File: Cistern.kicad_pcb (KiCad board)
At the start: 2 copper layers, 55.5 x 79.6 mm, 15 parts, among them J2 Gauge Stepper, J3 Power Connector, Q1 BD244C, SW1 WiFi reset, SW2 Water Sensor, U1 ULN2003A, U3 Boost Converter (5->20 V)

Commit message: Changing pin assignments to make things work
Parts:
- SW1: value WiFi reset -> WiFi reset switch
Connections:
- MCU1 pad 13: unconnected-(MCU1-GPIO13-Pad13) -> Net-(MCU1-GPIO13)
- MCU1 pad 5: Net-(MCU1-GPIO35) -> unconnected-(MCU1-GPIO35-Pad5)
- U1 pad 1: Net-(MCU1-GPIO27) -> Net-(MCU1-GPIO13)
- U1 pad 2: Net-(MCU1-GPIO26) -> Net-(MCU1-GPIO27)
- U1 pad 3: Net-(MCU1-GPIO25) -> Net-(MCU1-GPIO26)
- U1 pad 4: Net-(MCU1-GPIO33) -> Net-(MCU1-GPIO25)
- U1 pad 5: Net-(MCU1-GPIO32) -> Net-(MCU1-GPIO33)
- U1 pad 6: Net-(MCU1-GPIO35) -> Net-(MCU1-GPIO32)
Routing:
- net Net-(MCU1-GPIO13): track 0.00 -> 17.8 mm
- net Net-(MCU1-GPIO35): track 10.2 -> 0.00 mm
- net Net-(D2-A): track 10.8 -> 8.94 mm
- net Net-(MCU1-GPIO27): track 10.2 -> 11.2 mm
- net Net-(MCU1-GPIO25): track 10.2 -> 11.2 mm
- net Net-(MCU1-GPIO33): track 10.2 -> 11.2 mm
- net Net-(MCU1-GPIO32): track 10.2 -> 11.2 mm
- net Net-(MCU1-GPIO26): track 10.2 -> 11.2 mm
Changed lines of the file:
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@@
 	(net 15 "unconnected-(MCU1-GPIO21-Pad20)")
 	(net 16 "unconnected-(MCU1-RX2-Pad25)")
-	(net 17 "Net-(MCU1-GPIO35)")
+	(net 17 "Net-(MCU1-GPIO13)")
 	(net 18 "unconnected-(MCU1-VN-Pad3)")
 	(net 19 "unconnected-(MCU1-3V3-Pad30)")
@@
 	(net 24 "unconnected-(MCU1-GPIO23-Pad16)")
 	(net 25 "unconnected-(MCU1-GPIO5-Pad23)")
-	(net 26 "unconnected-(MCU1-GPIO13-Pad13)")
+	(net 26 "unconnected-(MCU1-GPIO35-Pad5)")
 	(net 27 "unconnected-(MCU1-TX0-Pad18)")
 	(net 28 "unconnected-(MCU1-TX2-Pad24)")
@@
 			)
 		)
-		(property "Value" "WiFi reset"
+		(property "Value" "WiFi reset switch"
 			(at 2.54 -2.54 180)
 			(layer "F.Fab")
@@
 			(layers "*.Cu" "*.Mask")
 			(remove_unused_layers no)
-			(net 20 "Net-(MCU1-GPIO27)")
+			(net 17 "Net-(MCU1-GPIO13)")
 			(pinfunction "I1")
 			(pintype "input")
@@
 			(layers "*.Cu" "*.Mask")
 			(remove_unused_layers no)
-			(net 11 "Net-(MCU1-GPIO26)")
+			(net 20 "Net-(MCU1-GPIO27)")
 			(pinfunction "I2")
 			(pintype "input")
@@
 			(layers "*.Cu" "*.Mask")
 			(remove_unused_layers no)
-			(net 35 "Net-(MCU1-GPIO25)")
+			(net 11 "Net-(MCU1-GPIO26)")
 			(pinfunction "I3")
 			(pintype "input")
@@
 			(layers "*.Cu" "*.Mask")
 			(remove_unused_layers no)
-			(net 12 "Net-(MCU1-GPIO33)")
+			(net 35 "Net-(MCU1-GPIO25)")
 			(pinfunction "I4")
 			(pintype "input")
@@
 			(layers "*.Cu" "*.Mask")
 			(remove_unused_layers no)
-			(net 21 "Net-(MCU1-GPIO32)")
+			(net 12 "Net-(MCU1-GPIO33)")
 			(pinfunction "I5")
 			(pintype "input")
@@
 			(layers "*.Cu" "*.Mask")
 			(remove_unused_layers no)
-			(net 17 "Net-(MCU1-GPIO35)")
+			(net 21 "Net-(MCU1-GPIO32)")
 			(pinfunction "I6")
 			(pintype "input")
@@
 			(layers "*.Cu" "*.Mask")
 			(remove_unused_layers no)
-			(net 17 "Net-(MCU1-GPIO35)")
+			(net 26 "unconnected-(MCU1-GPIO35-Pad5)")
 			(pinfunction "GPIO35")
-			(pintype "bidirectional")
+			(pintype "bidirectional+no_connect")
 		)
 		(pad "6" thru_hole circle
@@
 			(layers "*.Cu" "*.Mask")
 			(remove_unused_layers no)
-			(net 26 "unconnected-(MCU1-GPIO13-Pad13)")
+			(net 17 "Net-(MCU1-GPIO13)")
 			(pinfunction "GPIO13")
-			(pintype "bidirectional+no_connect")
+			(pintype "bidirectional")
 		)
 		(pad "14" thru_hole circle
@@
 	(segment
 		(start 76.2 59.06)
-		(end 76.2 55.88)
+		(end 80.64 59.06)
 		(width 0.2)
 		(layer "B.Cu")
@@
 	)
 	(segment
-		(start 76.2 55.88)
+		(start 80.64 59.06)
 		(end 83.82 55.88)
 		(width 0.2)
@@
 	)
 	(segment
-		(start 73.66 53.34)
-		(end 81.28 53.34)
-		(width 0.2)
-		(layer "B.Cu")
-		(net 6)
-	)
-	(segment
-		(start 81.28 53.34)
-		(end 81.28 50.8)
-		(width 0.2)
-		(layer "B.Cu")
-		(net 6)
-	)
-	(segment
 		(start 53.34 63.5)
 		(end 73.66 63.5)
@@
 	)
 	(segment
+		(start 73.66 55.88)
+		(end 73.66 63.5)
+		(width 0.2)
+		(layer "B.Cu")
+		(net 6)
+	)
+	(segment
 		(start 49.68 63.5)
 		(end 49.68 60.96)
@@
 	)
 	(segment
-		(start 73.66 63.5)
-		(end 73.66 53.34)
-		(width 0.2)
-		(layer "B.Cu")
-		(net 6)
-	)
-	(segment
 		(start 81.28 40.64)
 		(end 93.98 40.64)
@@
 	)
 	(segment
+		(start 81.28 50.8)
+		(end 81.28 55.88)
+		(width 0.2)
+		(layer "B.Cu")
+		(net 6)
+	)
+	(segment
+		(start 81.28 55.88)
+		(end 73.66 55.88)
+		(width 0.2)
+		(layer "B.Cu")
+		(net 6)
+	)
+	(segment
 		(start 58.42 68.58)
 		(end 58.42 78.74)
@@
 	)
 	(segment
-		(start 68.58 50.8)
-		(end 68.58 60.96)
+		(start 66.04 60.96)
+		(end 66.04 53.34)
+		(width 0.2)
+		(layer "B.Cu")
+		(net 11)
+	)
+	(segment
+		(start 66.04 53.34)
+		(end 68.58 50.8)
 		(width 0.2)
 		(layer "B.Cu")
@@
 	)
 	(segment
-		(start 63.5 50.8)
-		(end 63.5 60.96)
+		(start 60.96 60.96)
+		(end 60.96 53.34)
+		(width 0.2)
+		(layer "B.Cu")
+		(net 12)
+	)
+	(segment
+		(start 60.96 53.34)
+		(end 63.5 50.8)
 		(width 0.2)
 		(layer "B.Cu")
@@
 	)
 	(segment
-		(start 58.42 50.8)
-		(end 58.42 60.96)
+		(start 71.12 60.96)
+		(end 71.12 53.34)
+		(width 0.2)
+		(layer "B.Cu")
+		(net 17)
+	)
+	(segment
+		(start 78.74 53.34)
+		(end 78.74 50.8)
+		(width 0.2)
+		(layer "B.Cu")
+		(net 17)
+	)
+	(segment
+		(start 71.12 53.34)
+		(end 78.74 53.34)
 		(width 0.2)
 		(layer "B.Cu")
@@
 	)
 	(segment
-		(start 71.12 50.8)
-		(end 71.12 60.96)
+		(start 68.58 60.96)
+		(end 68.58 53.34)
+		(width 0.2)
+		(layer "B.Cu")
+		(net 20)
+	)
+	(segment
+		(start 68.58 53.34)
+		(end 71.12 50.8)
 		(width 0.2)
 		(layer "B.Cu")
@@
 	)
 	(segment
-		(start 60.96 50.8)
-		(end 60.96 60.96)
+		(start 58.42 53.34)
+		(end 60.96 50.8)
+		(width 0.2)
+		(layer "B.Cu")
+		(net 21)
+	)
+	(segment
+		(start 58.42 60.96)
+		(end 58.42 53.34)
 		(width 0.2)
 		(layer "B.Cu")
@@
 	)
 	(segment
-		(start 66.04 50.8)
-		(end 66.04 60.96)
+		(start 63.5 53.34)
+		(end 66.04 50.8)
+		(width 0.2)
+		(layer "B.Cu")
+		(net 35)
+	)
+	(segment
+		(start 63.5 60.96)
+		(end 63.5 53.34)
 		(width 0.2)
 		(layer "B.Cu")

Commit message: Changing assignments some more and updating board design
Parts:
- moved MCU1 47.9 mm to (88.9, 25.4), turned to -90 degrees
- moved SW2 12.7 mm to (78.7, 55.9), turned to -90 degrees
- moved R4 9.16 mm to (58.4, 91.4)
- moved R2 7.62 mm to (71.1, 88.9)
- moved Q1 5.68 mm to (71.1, 94.0), turned to 180 degrees
- moved D2 5.08 mm to (91.4, 55.9)
- moved J2 3.59 mm to (68.6, 76.2)
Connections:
- MCU1 pad 10: Net-(MCU1-GPIO27) -> unconnected-(MCU1-GPIO27-Pad10)
- MCU1 pad 13: Net-(MCU1-GPIO13) -> unconnected-(MCU1-GPIO13-Pad13)
- MCU1 pad 14: GND -> unconnected-(MCU1-GND-Pad14)
- MCU1 pad 20: unconnected-(MCU1-GPIO21-Pad20) -> Net-(MCU1-GPIO21)
- MCU1 pad 21: unconnected-(MCU1-GPIO19-Pad21) -> Net-(MCU1-GPIO19)
- MCU1 pad 24: unconnected-(MCU1-TX2-Pad24) -> Net-(MCU1-TX2)
- MCU1 pad 25: unconnected-(MCU1-RX2-Pad25) -> Net-(MCU1-RX2)
- MCU1 pad 26: Net-(D2-K) -> Net-(MCU1-GPIO4)
- MCU1 pad 6: Net-(MCU1-GPIO32) -> unconnected-(MCU1-GPIO32-Pad6)
- MCU1 pad 7: Net-(MCU1-GPIO33) -> Net-(D2-K)
- MCU1 pad 8: Net-(MCU1-GPIO25) -> unconnected-(MCU1-GPIO25-Pad8)
- SW1 pad 1: Net-(MCU1-GPIO18) -> Net-(MCU1-GPIO26)
- SW2 pad 1: Net-(MCU1-GPIO15) -> Net-(MCU1-GPIO21)
- U1 pad 1: Net-(MCU1-GPIO13) -> Net-(MCU1-GPIO19)
- U1 pad 11: Net-(J2-Pin_4) -> Net-(BZ1--)
- U1 pad 12: Net-(J2-Pin_3) -> Net-(J2-Pin_4)
- U1 pad 13: Net-(J2-Pin_2) -> Net-(J2-Pin_3)
- U1 pad 14: Net-(J2-Pin_1) -> Net-(J2-Pin_2)
- U1 pad 15: Net-(BZ1--) -> Net-(J2-Pin_1)
- U1 pad 2: Net-(MCU1-GPIO27) -> Net-(MCU1-GPIO18)
- U1 pad 3: Net-(MCU1-GPIO26) -> Net-(MCU1-TX2)
- U1 pad 4: Net-(MCU1-GPIO25) -> Net-(MCU1-RX2)
- U1 pad 5: Net-(MCU1-GPIO33) -> Net-(MCU1-GPIO4)
- U1 pad 6: Net-(MCU1-GPIO32) -> Net-(MCU1-GPIO15)
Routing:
- net GND: track 198.1 -> 241.2 mm
- net Net-(MCU1-GPIO18): track 51.4 -> 12.3 mm
- net Net-(MCU1-GPIO26): track 11.2 -> 49.6 mm
- net Net-(MCU1-GPIO15): track 43.2 -> 10.2 mm
- net +5V: track 172.7 -> 139.7 mm
- net Net-(BZ1--): track 53.3 -> 30.5 mm
- net Net-(MCU1-GPIO13): track 17.8 -> 0.00 mm
- net Net-(MCU1-GPIO19): track 0.00 -> 12.3 mm
- net Net-(MCU1-RX2): track 0.00 -> 11.2 mm
- net Net-(MCU1-GPIO27): track 11.2 -> 0.00 mm
- net Net-(MCU1-GPIO25): track 11.2 -> 0.00 mm
- net Net-(MCU1-GPIO4): track 0.00 -> 11.2 mm
- net Net-(MCU1-GPIO33): track 11.2 -> 0.00 mm
- net Net-(MCU1-GPIO32): track 11.2 -> 0.00 mm
- net Net-(MCU1-TX2): track 0.00 -> 11.2 mm
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
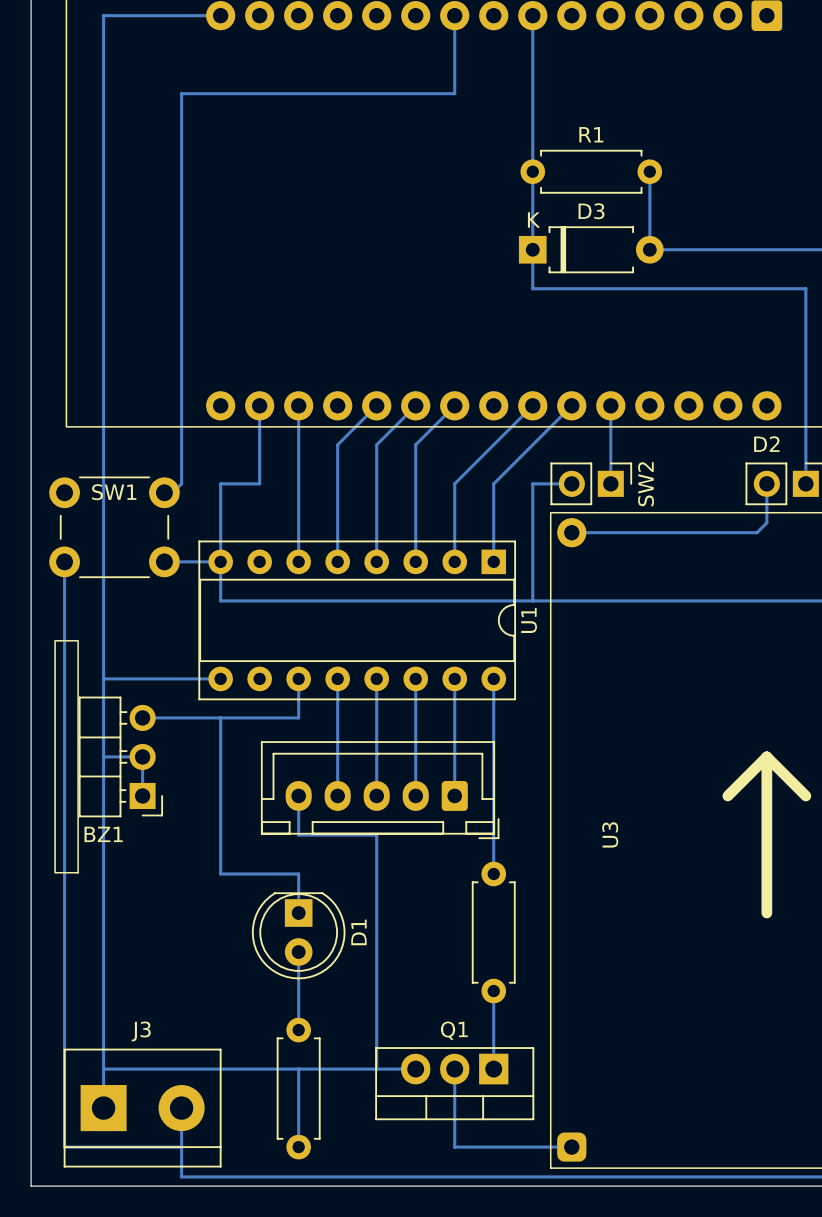
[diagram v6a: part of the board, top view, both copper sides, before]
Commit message: Adding gauge calibration sensor
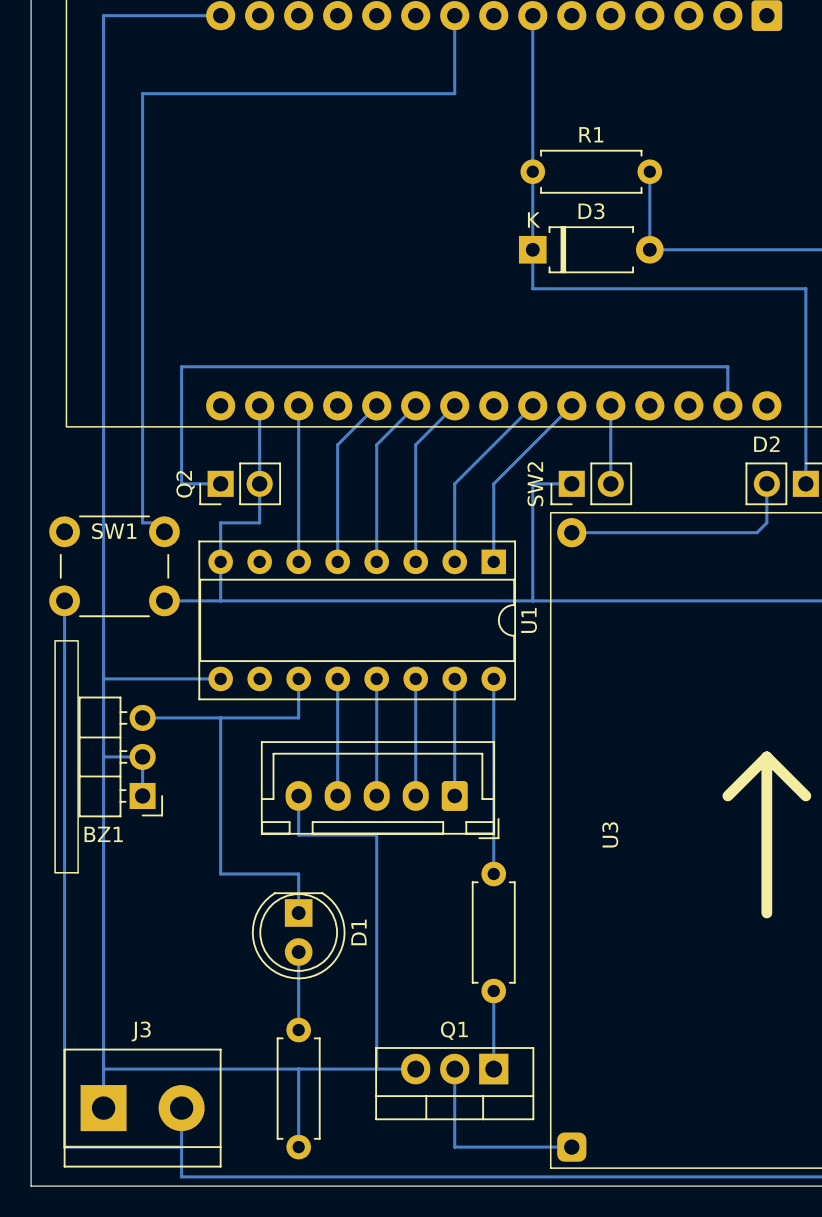
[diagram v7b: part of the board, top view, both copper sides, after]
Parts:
- added Q2: Gauge Calibration, Connector_PinHeader_2.54mm:PinHeader_1x02_P2.54mm_Vertical, F.Cu at (53.3, 55.9)
- SW1: value WiFi reset switch -> WiFi reset
- moved SW1 2.54 mm to (43.2, 59.0)
- moved SW2 2.54 mm to (76.2, 55.9), turned to 90 degrees
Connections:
- MCU1 pad 17: unconnected-(MCU1-GPIO22-Pad17) -> Net-(MCU1-GPIO22)
- SW2 pad 1: Net-(MCU1-GPIO21) -> GND
- SW2 pad 2: GND -> Net-(MCU1-GPIO21)
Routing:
- net Net-(MCU1-GPIO22): track 0.00 -> 48.3 mm
- net Net-(MCU1-GPIO26): track 49.6 -> 55.0 mm
- net GND: track 241.2 -> 238.7 mm
